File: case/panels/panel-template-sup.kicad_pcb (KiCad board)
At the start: 2 copper layers, 100 x 190 mm, 4 parts

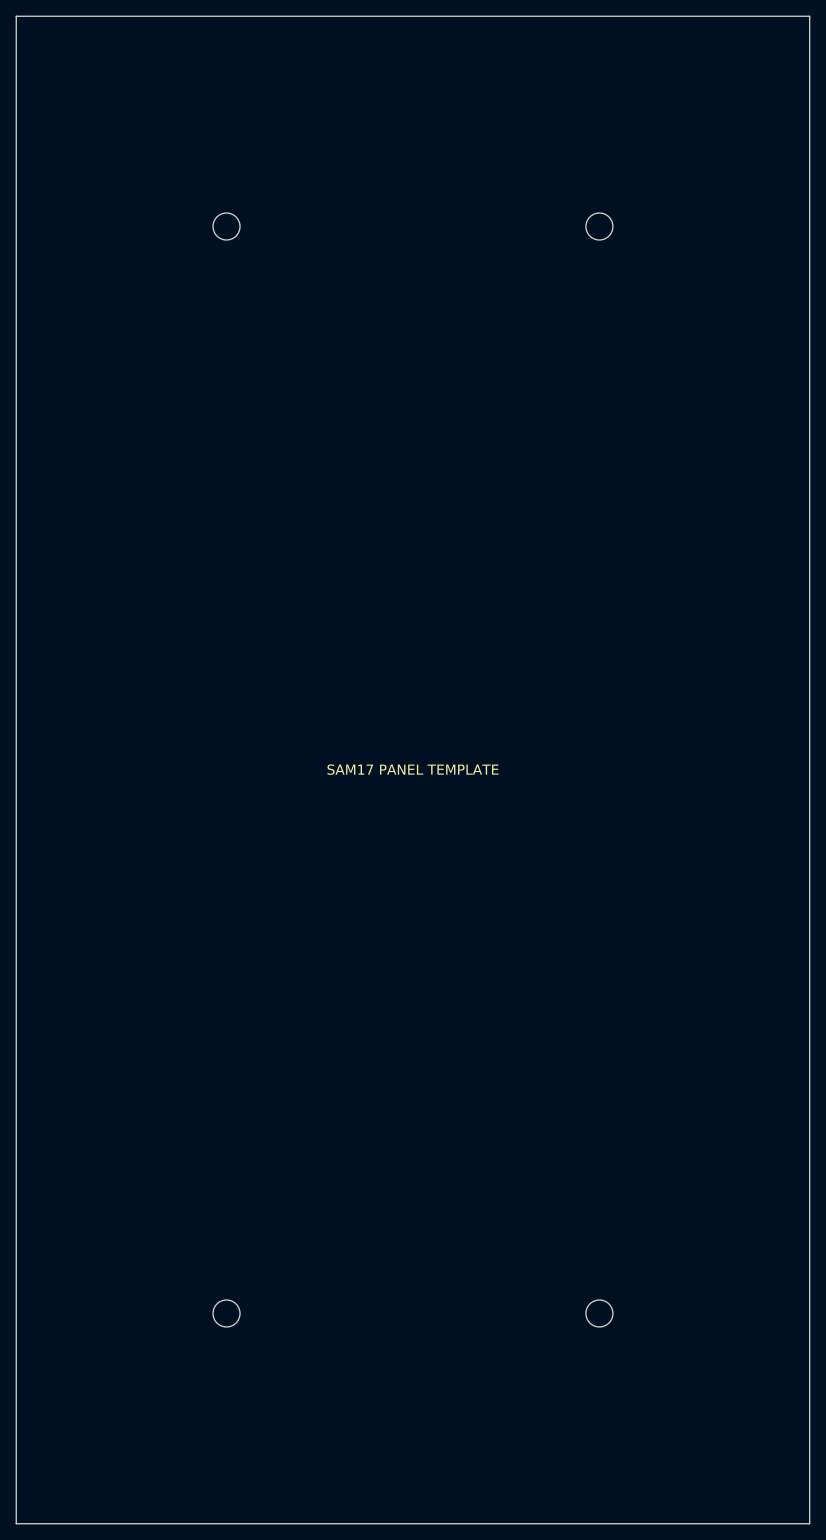
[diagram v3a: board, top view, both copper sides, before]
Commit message: Case: la fila de arriba tambien pasa a 3U, y los insets se vuelven cuatro
Samuel pidio el mismo tratamiento en la seccion de arriba. Apretar sus insets
no le quitaba ni un milimetro -- su cara la fijaba el panel de 190, no el
estandar --, asi que el "mismo tratamiento" solo significa una cosa: que esa
fila sea EUROrack de verdad y se dimensione desde la cota, como la de abajo.

  alto_panel_sup  190 -> 128.5   (PCB 3U, igual que la de abajo)
  sep_railes_sup  137 -> 122.5   (el estandar)
  alto_cara_sup   190 -> 170.0   (DERIVADO: 122.5 + 24.5 + 23)

  alto total  296.7 -> 282.5
  fondo       331.8 -> 317.6

CUATRO INSETS, uno por punta de cara. Habia un `inset_tornillo` que servia
para todo y ya no da: cada punta llega a una esquina distinta del contorno y
lo que manda en cada una es cuanto acrilico se come SU curva. El patron es
siempre tangente + rail/2 + material, y lo unico que cambia es la tangente:

  inferior / frente   punta redondeada   14.0 + 10 + 2.5 = 26.5
  inferior / valle    pico    (r=5)       2.6 + 10 + 2.4 = 15
  superior / valle    valle   (r=30)     12.4 + 10 + 2.1 = 24.5
  superior / remate   punta redondeada   11.0 + 10 + 2.0 = 23

Por eso la cara de arriba sale 6 mm mas larga que la de abajo con el MISMO
estandar dentro: su curva del valle lleva radio_valle = 30 -- el redondeo
suave que pidio Samuel -- y esa tangente se come 12.4 mm de cara contra los
2.6 del pico de enfrente. El acabado se paga en altura y ahora esta escrito
cuanto cuesta.

Un fallo latente que salio por el camino: pts_perfil() calculaba yt con
alto_panel_sup en vez de alto_cara_sup. Era inofensivo mientras cara y panel
valian lo mismo arriba (190 = 190) y habria mentido 41.5 mm en cuanto dejaran
de valerlo -- que es exactamente lo que pasa en este commit. El .scad habria
dibujado un costado que ni el budget ni el DXF esperaban.

build_template.py: las dos filas se taladran ya con las cotas de EUROrack
(3.0 arriba/abajo, 7.5 del canto izquierdo), asi que las dos plantillas s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
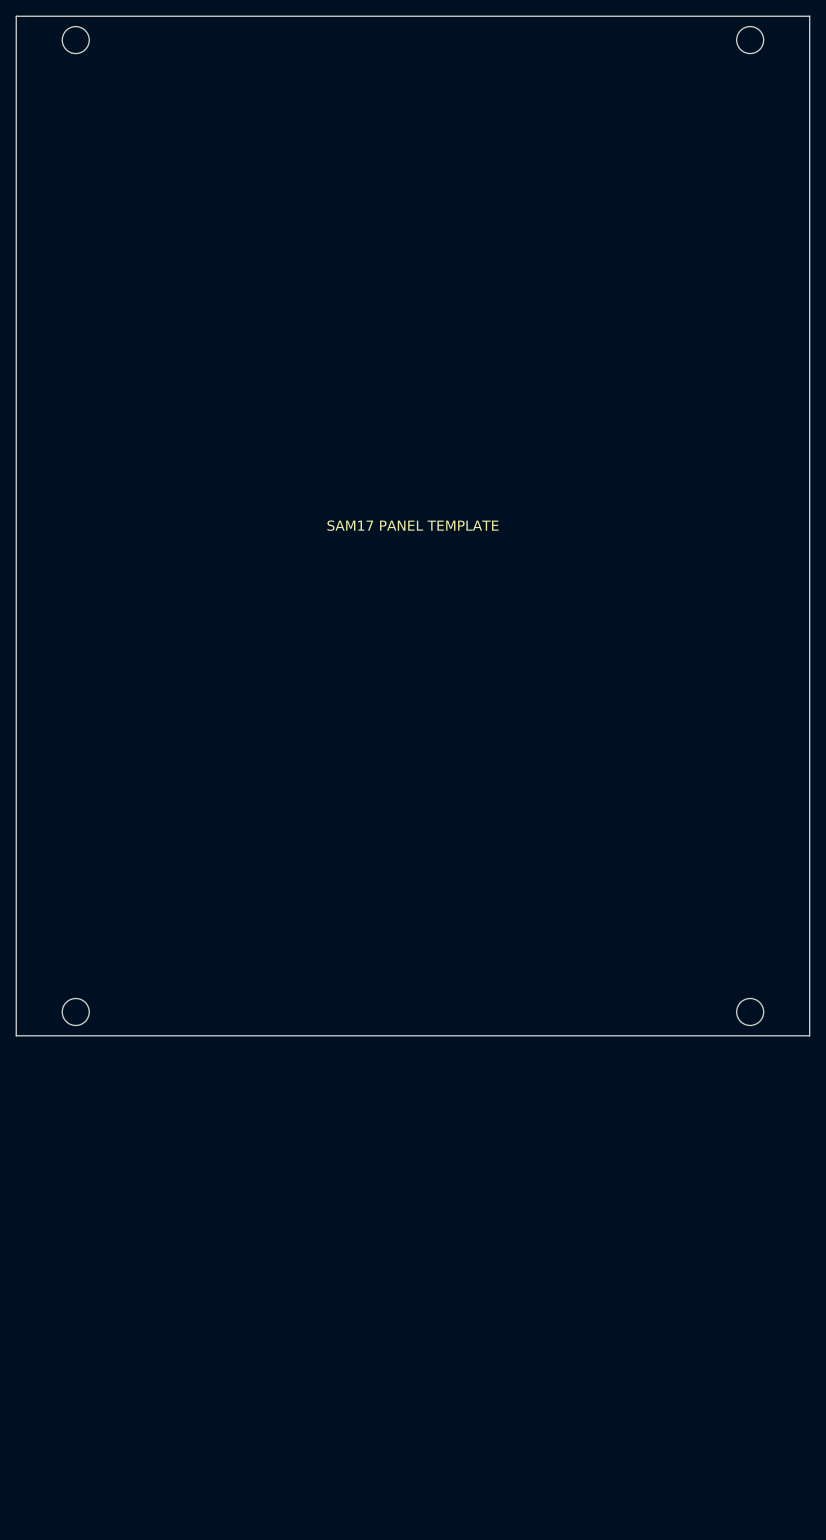
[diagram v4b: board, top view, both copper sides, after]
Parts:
- removed the ? at (73.5, 26.5)
- removed the ? at (26.5, 26.5)
- removed the ? at (73.5, 163.5)
- removed the ? at (26.5, 163.5)
- added ?: , , F.Cu at (92.5, 125.5)
- added ?: , , F.Cu at (7.50, 125.5)
- added ?: , , F.Cu at (7.50, 3.00)
- added ?: , , F.Cu at (92.5, 3.00)
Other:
- board size 100 x 190 mm -> 100 x 128.5 mm
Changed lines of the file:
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@@
 	(footprint ""
 		(layer "F.Cu")
-		(at 73.5 26.5)
-		(property "Reference" ""
-			(at 0 0 0)
-			(layer "F.SilkS")
-			(effects
-				(font
-					(size 1.27 1.27)
-				)
-			)
-		)
-		(property "Value" ""
-			(at 0 0 0)
-			(layer "F.Fab")
-			(effects
-				(font
-					(size 1.27 1.27)
-				)
-			)
-		)
-		(property "Datasheet" ""
-			(at 0 0 0)
-			(layer "F.Fab")
-			(hide yes)
-			(effects
-				(font
-					(size 1.27 1.27)
-				)
-			)
-		)
-		(property "Description" ""
-			(at 0 0 0)
-			(layer "F.Fab")
-			(hide yes)
-			(effects
-				(font
-					(size 1.27 1.27)
-				)
-			)
-		)
-		(duplicate_pad_numbers_are_jumpers no)
-		(pad "" np_thru_hole circle
-			(at 0 0)
-			(size 3.4 3.4)
-			(drill 3.4)
-			(layers "*.Cu" "*.Mask")
-		)
-		(embedded_fonts no)
-	)
-	(footprint ""
-		(layer "F.Cu")
-		(at 26.5 26.5)
-		(property "Reference" ""
-			(at 0 0 0)
-			(layer "F.SilkS")
-			(effects
-				(font
-					(size 1.27 1.27)
-				)
-			)
-		)
-		(property "Value" ""
-			(at 0 0 0)
-			(layer "F.Fab")
-			(effects
-				(font
-					(size 1.27 1.27)
-				)
-			)
-		)
-		(property "Datasheet" ""
-			(at 0 0 0)
-			(layer "F.Fab")
-			(hide yes)
-			(effects
-				(font
-					(size 1.27 1.27)
-				)
-			)
-		)
-		(property "Description" ""
-			(at 0 0 0)
-			(layer "F.Fab")
-			(hide yes)
-			(effects
-				(font
-					(size 1.27 1.27)
-				)
-			)
-		)
-		(duplicate_pad_numbers_are_jumpers no)
-		(pad "" np_thru_hole circle
-			(at 0 0)
-			(size 3.4 3.4)
-			(drill 3.4)
-			(layers "*.Cu" "*.Mask")
-		)
-		(embedded_fonts no)
-	)
-	(footprint ""
-		(layer "F.Cu")
-		(at 73.5 163.5)
-		(property "Reference" ""
-			(at 0 0 0)
-			(layer "F.SilkS")
-			(effects
-				(font
-					(size 1.27 1.27)
-				)
-			)
-		)
-		(property "Value" ""
-			(at 0 0 0)
-			(layer "F.Fab")
-			(effects
-				(font
-					(size 1.27 1.27)
-				)
-			)
-		)
-		(property "Datasheet" ""
-			(at 0 0 0)
-			(layer "F.Fab")
-			(hide yes)
-			(effects
-				(font
-					(size 1.27 1.27)
-				)
-			)
-		)
-		(property "Description" ""
-			(at 0 0 0)
-			(layer "F.Fab")
-			(hide yes)
-			(effects
-				(font
-					(size 1.27 1.27)
-				)
-			)
-		)
-		(duplicate_pad_numbers_are_jumpers no)
-		(pad "" np_thru_hole circle
-			(at 0 0)
-			(size 3.4 3.4)
-			(drill 3.4)
-			(layers "*.Cu" "*.Mask")
-		)
-		(embedded_fonts no)
-	)
-	(footprint ""
-		(layer "F.Cu")
-		(at 26.5 163.5)
+		(at 92.5 125.5)
+		(property "Reference" ""
+			(at 0 0 0)
+			(layer "F.SilkS")
+			(effects
+				(font
+					(size 1.27 1.27)
+				)
+			)
+		)
+		(property "Value" ""
+			(at 0 0 0)
+			(layer "F.Fab")
+			(effects
+				(font
+					(size 1.27 1.27)
+				)
+			)
+		)
+		(property "Datasheet" ""
+			(at 0 0 0)
+			(layer "F.Fab")
+			(hide yes)
+			(effects
+				(font
+					(size 1.27 1.27)
+				)
+			)
+		)
+		(property "Description" ""
+			(at 0 0 0)
+			(layer "F.Fab")
+			(hide yes)
+			(effects
+				(font
+					(size 1.27 1.27)
+				)
+			)
+		)
+		(duplicate_pad_numbers_are_jumpers no)
+		(pad "" np_thru_hole circle
+			(at 0 0)
+			(size 3.4 3.4)
+			(drill 3.4)
+			(layers "*.Cu" "*.Mask")
+		)
+		(embedded_fonts no)
+	)
+	(footprint ""
+		(layer "F.Cu")
+		(at 7.5 125.5)
+		(property "Reference" ""
+			(at 0 0 0)
+			(layer "F.SilkS")
+			(effects
+				(font
+					(size 1.27 1.27)
+				)
+			)
+		)
+		(property "Value" ""
+			(at 0 0 0)
+			(layer "F.Fab")
+			(effects
+				(font
+					(size 1.27 1.27)
+				)
+			)
+		)
+		(property "Datasheet" ""
+			(at 0 0 0)
+			(layer "F.Fab")
+			(hide yes)
+			(effects
+				(font
+					(size 1.27 1.27)
+				)
+			)
+		)
+		(property "Description" ""
+			(at 0 0 0)
+			(layer "F.Fab")
+			(hide yes)
+			(effects
+				(font
+					(size 1.27 1.27)
+				)
+			)
+		)
+		(duplicate_pad_numbers_are_jumpers no)
+		(pad "" np_thru_hole circle
+			(at 0 0)
+			(size 3.4 3.4)
+			(drill 3.4)
+			(layers "*.Cu" "*.Mask")
+		)
+		(embedded_fonts no)
+	)
+	(footprint ""
+		(layer "F.Cu")
+		(at 7.5 3)
+		(property "Reference" ""
+			(at 0 0 0)
+			(layer "F.SilkS")
+			(effects
+				(font
+					(size 1.27 1.27)
+				)
+			)
+		)
+		(property "Value" ""
+			(at 0 0 0)
+			(layer "F.Fab")
+			(effects
+				(font
+					(size 1.27 1.27)
+				)
+			)
+		)
+		(property "Datasheet" ""
+			(at 0 0 0)
+			(layer "F.Fab")
+			(hide yes)
+			(effects
+				(font
+					(size 1.27 1.27)
+				)
+			)
+		)
+		(property "Description" ""
+			(at 0 0 0)
+			(layer "F.Fab")
+			(hide yes)
+			(effects
+				(font
+					(size 1.27 1.27)
+				)
+			)
+		)
+		(duplicate_pad_numbers_are_jumpers no)
+		(pad "" np_thru_hole circle
+			(at 0 0)
+			(size 3.4 3.4)
+			(drill 3.4)
+			(layers "*.Cu" "*.Mask")
+		)
+		(embedded_fonts no)
+	)
+	(footprint ""
+		(layer "F.Cu")
+		(at 92.5 3)
 		(property "Reference" ""
 			(at 0 0 0)
@@
 	)
 	(gr_line
-		(start 0 190)
+		(start 0 128.5)
 		(end 0 0)
 		(stroke
@@
 	(gr_line
 		(start 100 0)
-		(end 100 190)
-		(stroke
-			(width 0.1)
-			(type default)
-		)
-		(layer "Edge.Cuts")
-	)
-	(gr_line
-		(start 100 190)
-		(end 0 190)
+		(end 100 128.5)
+		(stroke
+			(width 0.1)
+			(type default)
+		)
+		(layer "Edge.Cuts")
+	)
+	(gr_line
+		(start 100 128.5)
+		(end 0 128.5)
 		(stroke
 			(width 0.1)
@@
 	)
 	(gr_text "SAM17 PANEL TEMPLATE"
-		(at 50 95 0)
+		(at 50 64.25 0)
 		(layer "F.SilkS")
 		(effects

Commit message: Case: entra el riel EUROrack REAL; se acabo el supuesto que sostenia la silueta
Contesto StudioRacks (John, 2026-08-17) con dos planos y la cota que faltaba.
Todo lo que estaba marcado ASUMIDO en params.scad se cambia por medido.

QUE DICEN LOS PLANOS

  Riel     seccion 27.40 (fondo, hacia dentro) x 10.00 (alto, a lo largo del
           panel). Taladro de 4.5 para el M5 de punta a 13.70 de cada canto en
           fondo y 5.00 en alto: cae en el centroide.
  Mejilla  FLAT-S 133.00 x 30.50, dos M5 a 5.00 de cada punta -> 123.00 ENTRE
           CENTROS, eje a 13.80 del canto delantero. Los dos planos se
           confirman: 13.70 del riel contra 13.80 de la mejilla.

LOS DOS SUPUESTOS QUE CAEN

1. NO HAY 2020 DETRAS DE LAS CARAS. Se suponia que el riel EUROrack iria
   atornillado encima de un 2020; el plano ensena que se fija de punta con un
   M5 directo al acrilico. Los 2020 se quedan solo en el esqueleto, que es
   donde hacen estructura. El costado sigue con sus mismos taladros: lo que
   cambia es que ahora entran al riel y no a un perfil intermedio.

2. LA SEPARACION NO ES 122.50 SINO 123.00. Doepfer es el estandar de catalogo;
   el riel que se compra es el que atornilla. De ahi inset_er = 2.75 y no 3.0,
   que es la resta (128.5 - 123)/2 y no una eleccion.

   Consecuencia que hay que saber y queda escrita: un modulo de terceros con
   sus taladros a 3.0 queda 0.25 mm descentrado por lado. En taladro de 3.2
   sobre M3 hay 0.2 de juego radial, o sea que entra pero justo.

LO QUE MUEVE EN LA GEOMETRIA

  rail_er_alto/fondo/eje   nuevos: 10 / 27.4 / 13.7
  sep_railes_inf y sup     122.5 -> 123.0
  inset_er                 3.0   -> 2.75
  inset_inf_frente         26.5  -> 23.5
  inset_inf_valle          15    -> 10
  inset_sup_valle          24.5  -> 19.5
  inset_sup_remate         16    -> 15.75
  alto_frontal             28    -> 31
  alto_cara_inf            164.0 -> 156.5
  alto_cara_sup            163.0 -> 158.25

  alto   277.6 -> 271.1      fondo  298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
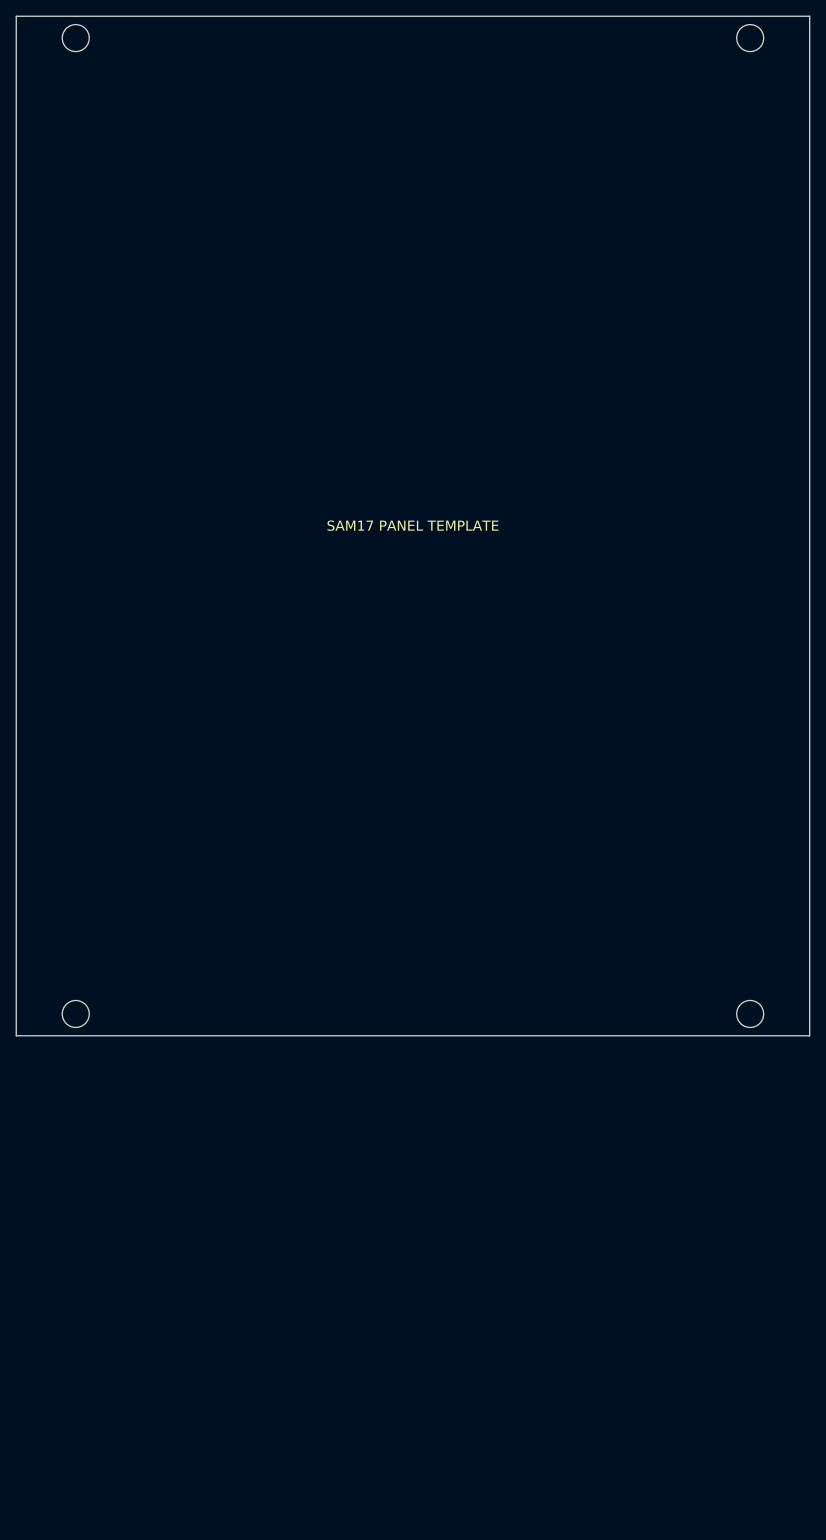
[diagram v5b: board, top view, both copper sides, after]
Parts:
- removed the ? at (92.5, 125.5)
- removed the ? at (7.50, 125.5)
- removed the ? at (7.50, 3.00)
- removed the ? at (92.5, 3.00)
- added ?: , , F.Cu at (92.5, 125.8)
- added ?: , , F.Cu at (92.5, 2.75)
- added ?: , , F.Cu at (7.50, 2.75)
- added ?: , , F.Cu at (7.50, 125.8)
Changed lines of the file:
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@@
 	(footprint ""
 		(layer "F.Cu")
-		(at 92.5 125.5)
+		(at 92.5 125.75)
 		(property "Reference" ""
 			(at 0 0 0)
@@
 	(footprint ""
 		(layer "F.Cu")
-		(at 7.5 125.5)
+		(at 92.5 2.75)
 		(property "Reference" ""
 			(at 0 0 0)
@@
 	(footprint ""
 		(layer "F.Cu")
-		(at 7.5 3)
+		(at 7.5 2.75)
 		(property "Reference" ""
 			(at 0 0 0)
@@
 	(footprint ""
 		(layer "F.Cu")
-		(at 92.5 3)
+		(at 7.5 125.75)
 		(property "Reference" ""
 			(at 0 0 0)
